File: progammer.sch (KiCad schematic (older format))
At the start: 76 parts, among them J5 USB_B_Micro, U1 ICE40HX4K-TQ144, U11 SN74LVC2G07DCKR, U13 SN74AXC4T245PWR, U14 MIC5365-3.3YC5, U16 SN74LVC2T45DCUR, U17 SN74LVC2T45DCUR, U18 SN74LVC2T45DCUR, U19 SN74LVC2T45DCUR, U3 93LCxxBT-I_OT, U4 FT2232H, U5 IS25LP080D, Y1 ECS-3225S33-120-FN-TR

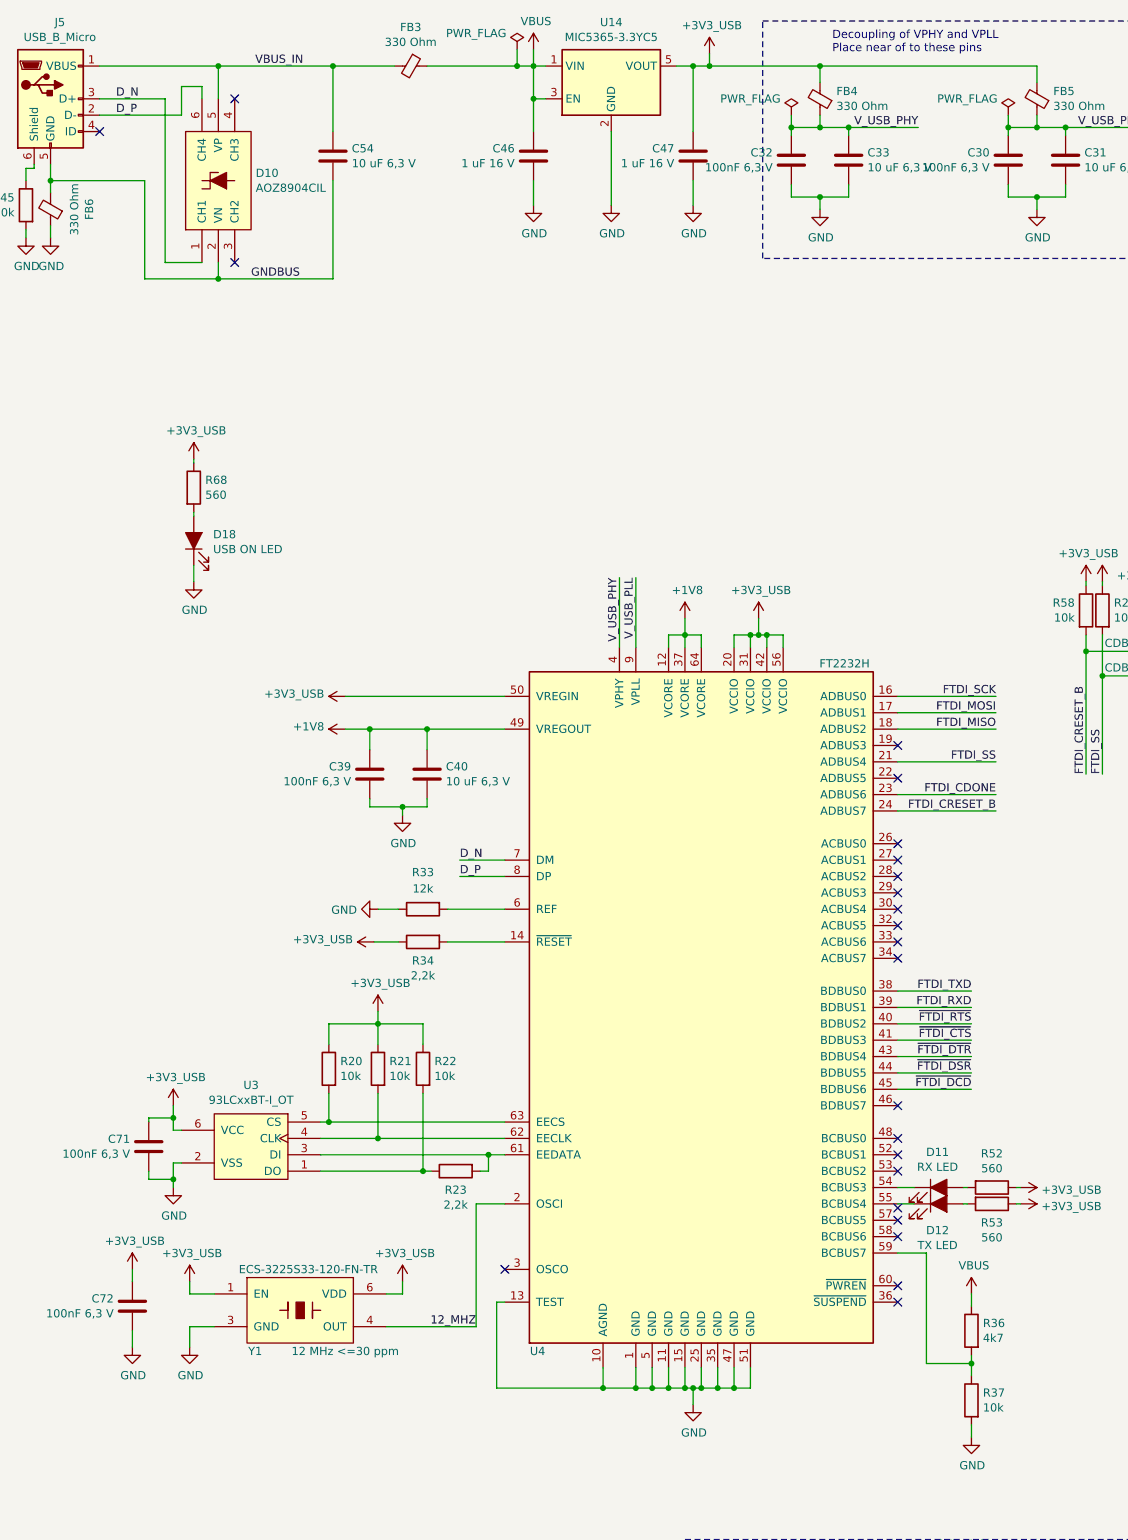
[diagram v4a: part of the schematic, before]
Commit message: Finished Silkscreen and added layer markings as specified by manufacturer
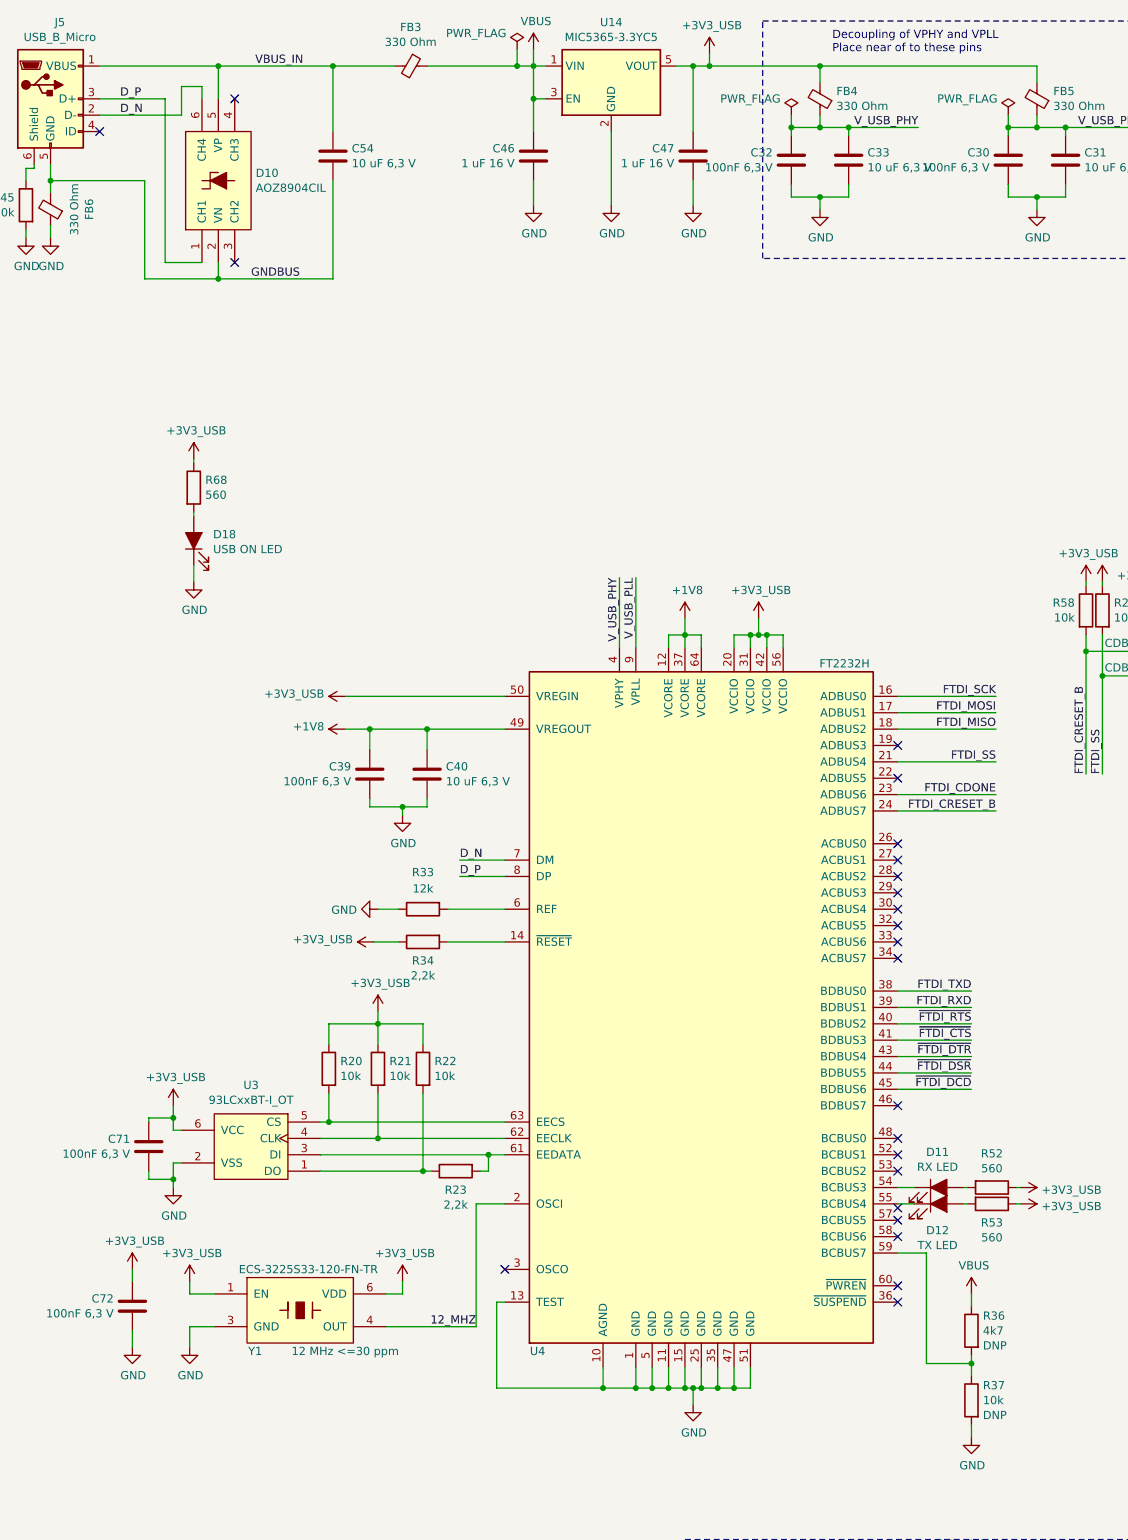
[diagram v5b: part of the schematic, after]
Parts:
- R36, R37: DNP (none) -> DNP
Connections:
- net D_N: now also D10.6 (CH4), J5.2 (D-); no longer D10.1 (CH1), J5.3 (D+)
- net D_P: now also D10.1 (CH1), J5.3 (D+); no longer D10.6 (CH4), J5.2 (D-)
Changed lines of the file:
@@
 Wire Wire Line
 	1650 1175 1150 1175
-Text Label 1250 1175 0    50   ~ 0
+Text Label 1275 1075 0    50   ~ 0
 D_P
-Text Label 1250 1075 0    50   ~ 0
+Text Label 1275 1175 0    50   ~ 0
 D_N
 $Comp
@@
 U 1 1 5CF17670
 P 6475 9025
-F 0 "R37" H 6405 9071 50  0000 R CNN
-F 1 "10k" H 6405 8980 50  0000 R CNN
+F 0 "R37" H 6405 9116 50  0000 R CNN
+F 1 "10k" H 6405 9025 50  0000 R CNN
 F 2 "Resistor_SMD:R_0603_1608Metric" V 6405 9025 50  0001 C CNN
 F 3 "~" H 6475 9025 50  0001 C CNN
+F 4 "DNP" H 6405 8934 50  0000 R CNN "DNP"
 	1    6475 9025
 	-1   0    0    -1
@@
 U 1 1 5CF17A14
 P 6475 8600
-F 0 "R36" H 6405 8646 50  0000 R CNN
-F 1 "4k7" H 6405 8555 50  0000 R CNN
+F 0 "R36" H 6405 8691 50  0000 R CNN
+F 1 "4k7" H 6405 8600 50  0000 R CNN
 F 2 "Resistor_SMD:R_0603_1608Metric" V 6405 8600 50  0001 C CNN
 F 3 "~" H 6475 8600 50  0001 C CNN
+F 4 "DNP" H 6405 8509 50  0000 R CNN "DNP"
 	1    6475 8600
 	-1   0    0    -1

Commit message: More complete BOM
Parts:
- C31, C33, C40, C54, C55, C65: Description CAP CER 10UF 6.3V X5R 0603 -> CAP CER 10UF 6.3V X5R 0603
- D11, D12, D18: Description (none) -> LED RED DIFFUSED 1608 SMD; Digikey (none) -> SML-D12U1WT86CT-ND; Mfg Name (none) -> Rohm Semiconductor; Mfg Part Num (none) -> SML-D12U1WT86; Spec (none) -> Any
- R20, R21, R22, R29, R37, R38, R39, R43, R44, R45, R58, R59: Description (none) -> RES 10K OHM 5% 1/10W 0603; Digikey (none) -> RMCF0603JT10K0CT-ND; Mfg Name (none) -> Stackpole Electronics Inc; Mfg Part Num (none) -> RMCF0603JT10K0; Spec (none) -> Any
- R23, R34: Description (none) -> RES SMD 2.2K OHM 1% 1/10W 0603; Digikey (none) -> 311-2.20KHRCT-ND; Mfg Name (none) -> Yageo; Mfg Part Num (none) -> RC0603FR-072K2L; Spec (none) -> Any
- R33: Description (none) -> RES SMD 12K OHM 5% 1/10W 0603; Digikey (none) -> 311-12KGRCT-ND; Mfg Name (none) -> Yageo; Mfg Part Num (none) -> RC0603JR-0712KL; Spec (none) -> Any
- R52, R53, R68: Description (none) -> RES 560 OHM 5% 1/8W 0603; Digikey (none) -> 2019-RK73B1JTTD561JCT-ND; Mfg Name (none) -> KOA Speer Electronics, Inc.; Mfg Part Num (none) -> RK73B1JTTD561J; Spec (none) -> Any
